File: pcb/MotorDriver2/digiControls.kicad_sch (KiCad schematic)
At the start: 11 parts, among them U3 XIAO-ESP32-C5-DIP, U4 MCP2562FDT-H/SN, U5 MCP2562FDT-H/SN

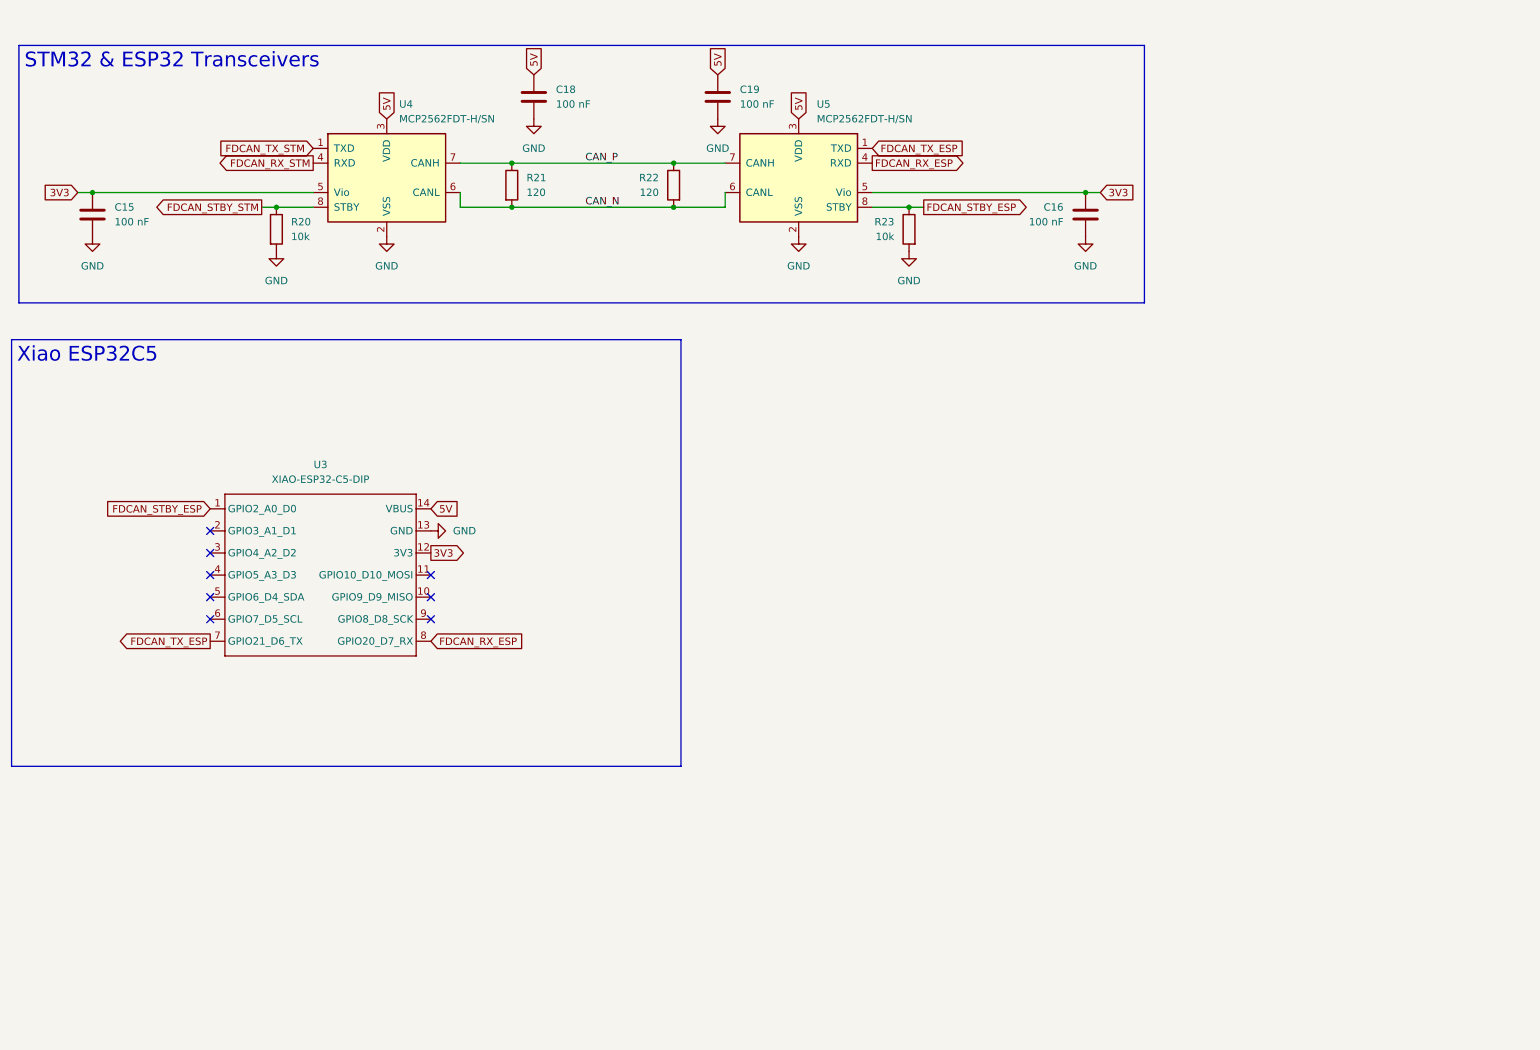
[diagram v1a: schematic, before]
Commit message: added ideal diode protection
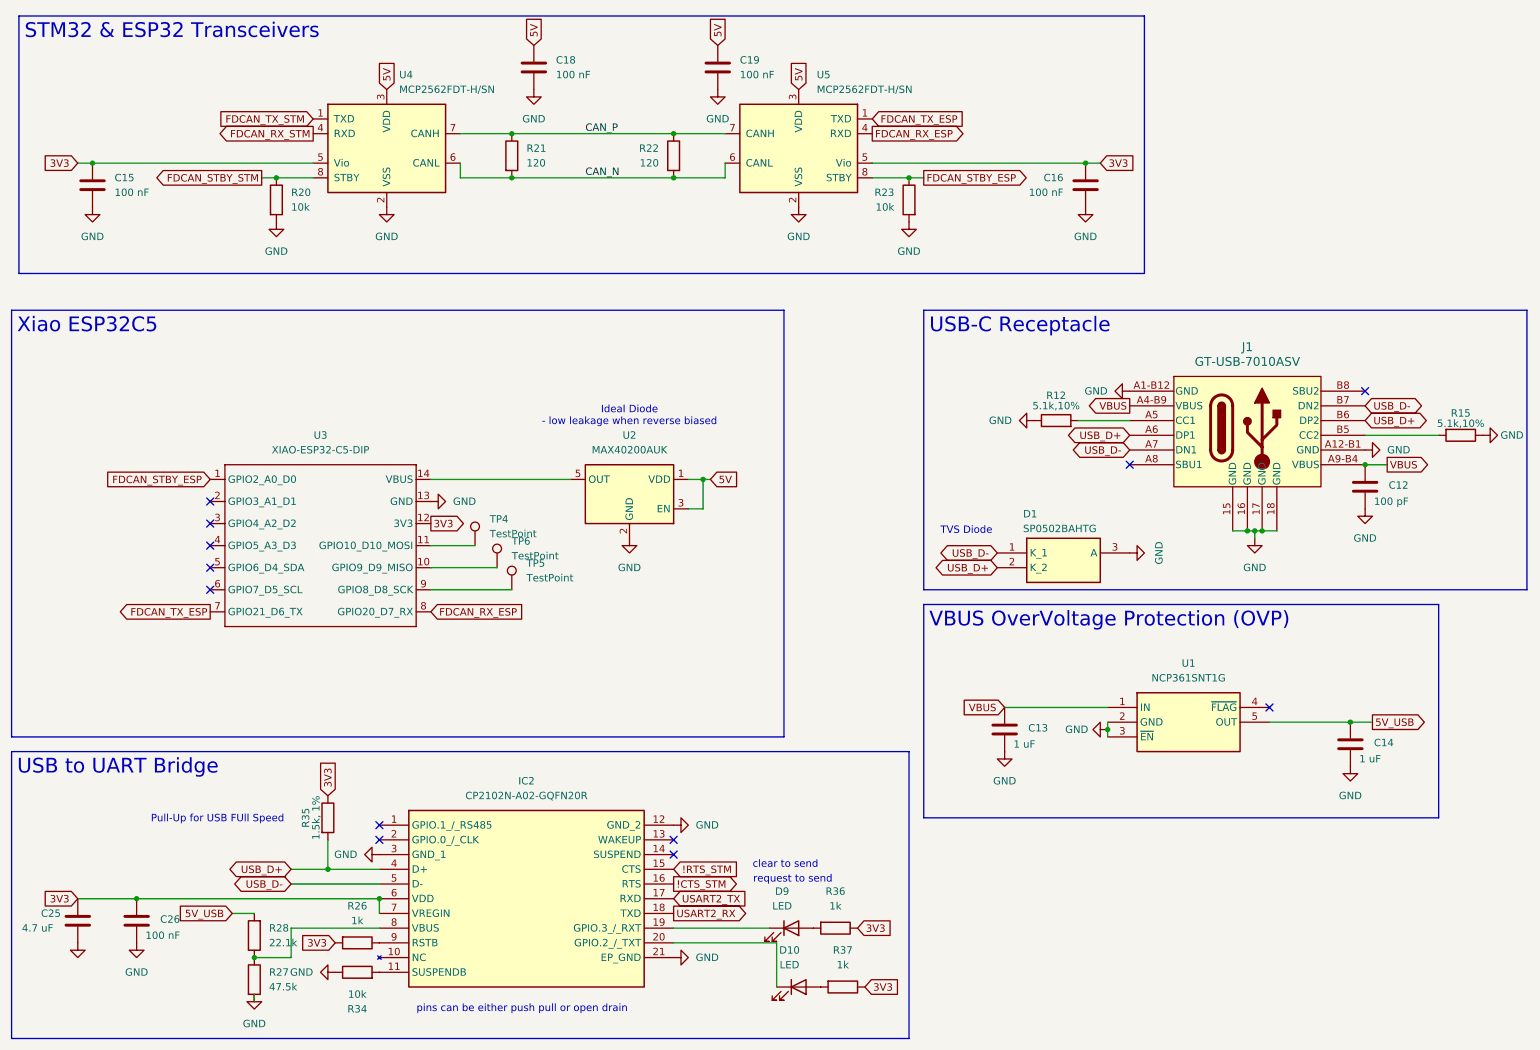
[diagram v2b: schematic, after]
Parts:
- added C12: 100 pF, Capacitor_SMD:C_0402_1005Metric, symbol Device:C
- added C13, C14: 1 uF, Capacitor_SMD:C_0603_1608Metric, symbol Device:C
- added C25: 4.7 uF, Capacitor_SMD:C_0603_1608Metric, symbol Device:C
- added C26: 100 nF, Capacitor_SMD:C_0402_1005Metric, symbol Device:C
- added D1: SP0502BAHTG, CapstoneFootprints:SOT95P237X112-3N, symbol pcb:SP0502BAHTG
- added D10, D9: LED, Diode_SMD:D_0402_1005Metric, symbol Device:LED
- added IC2: CP2102N-A02-GQFN20R, CapstoneFootprints:CP2102NA02GQFN20, symbol pcb:CP2102N-A02-GQFN20R
- added J1: GT-USB-7010ASV, footprintLib:USB4110-GF-A_GCT, symbol pcb:USB4110-GF-A
- added R12, R15: 5.1k,10%, Resistor_SMD:R_0402_1005Metric, symbol Device:R
- added R26, R36, R37: 1k, Resistor_SMD:R_0402_1005Metric, symbol Device:R
- added R27: 47.5k, Resistor_SMD:R_0402_1005Metric, symbol Device:R
- added R28: 22.1k, Resistor_SMD:R_0402_1005Metric, symbol Device:R
- added R34: 10k, Resistor_SMD:R_0402_1005Metric, symbol Device:R
- added R35: 1.5k, 1%, Resistor_SMD:R_0402_1005Metric, symbol Device:R
- added TP4, TP5, TP6: TestPoint, TestPoint:TestPoint_Pad_1.0x1.0mm, symbol Connector:TestPoint
- added U1: NCP361SNT1G, footprintLib:SOT95P275X110-5N, symbol pcb:NCP361SNT1G
- added U2: MAX40200AUK, Package_TO_SOT_SMD:SOT-23-5, symbol Analog_Switch:MAX40200AUK
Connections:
- net 3V3: now also C25.2, C26.2, IC2.6 (VDD), IC2.7 (VREGIN), R26.2, R35.1, R36.1, R37.1
- net 5V: now also U2.1 (VDD), U2.3 (EN); no longer U3.14 (VBUS)
- net GND: now also C12.1, C13.1, C14.1, C25.1, C26.1, D1.3 (A), IC2.12 (GND_2), IC2.21 (EP_GND), IC2.3 (GND_1), J1.15 (GND), J1.16 (GND), J1.17 (GND), J1.18 (GND), J1.A1-B12 (GND), J1.A12-B1 (GND), R12.1, R15.1, R27.2, R34.1, U1.2 (GND), U1.3 (~{EN}), U2.2 (GND)
- net at U3.10 (GPIO9_D9_MISO): now also TP6.1
- net at U3.11 (GPIO10_D10_MOSI): now also TP4.1
- net at U3.9 (GPIO8_D8_SCK): now also TP5.1
- new net: J1.A5 (CC1), R12.2
- new net: IC2.11 (SUSPENDB), R34.2
- new net: D9.1 (K), IC2.19 (GPIO.3_/_RXT)
- new net: D10.1 (K), IC2.20 (GPIO.2_/_TXT)
- new net: IC2.8 (VBUS), R27.1, R28.1
- new net: IC2.9 (RSTB), R26.1
- new net: J1.B5 (CC2), R15.2
- new net: D9.2 (A), R36.2
- new net: D10.2 (A), R37.2
- new net: U2.5 (OUT), U3.14 (VBUS)
- new net !CTS_STM: IC2.16 (RTS)
- new net !RTS_STM: IC2.15 (CTS)
- new net 5V_USB: C14.2, R28.2, U1.5 (OUT)
- new net USART2_RX: IC2.18 (TXD)
- new net USART2_TX: IC2.17 (RXD)
- new net USB_D+: D1.2 (K_2), IC2.4 (D+), J1.A6 (DP1), J1.B6 (DP2), R35.2
- new net USB_D-: D1.1 (K_1), IC2.5 (D-), J1.A7 (DN1), J1.B7 (DN2)
- new net VBUS: C12.2, C13.2, J1.A4-B9 (VBUS), J1.A9-B4 (VBUS), U1.1 (IN)
- no-connect marks 8 -> 12
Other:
- note added: "Ideal Diode - low leakage when reverse biased"
- note added: "Pull-Up for USB FUll Speed"
- note added: "TVS Diode"
- note added: "clear to send"
- note added: "pins can be either push pull or open drain"
- note added: "request to send"
- moved on the sheet: C15, C16, C18, C19, R20, R21, R22, R23, U3, U4, U5

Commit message: Laying out PCB
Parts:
- removed TP4, TP5, TP6: TestPoint, TestPoint:TestPoint_Pad_1.0x1.0mm, symbol Connector:TestPoint
- C13, C14: LCSC (none) -> C15849
- J1: footprint footprintLib:USB4110-GF-A_GCT -> CapstoneFootprints:USB4110-GF-A_GCT
- R12, R15: LCSC (none) -> C25905
- R21, R22: LCSC (none) -> C25079
- U1: footprint footprintLib:SOT95P275X110-5N -> CapstoneFootprints:SOT95P275X110-5N
- U3: footprint footprintLib:XIAO-ESP32-C5-DIP -> CapstoneFootprints:XIAO-ESP32-C5-DIP
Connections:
- no-connect marks 12 -> 15

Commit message: Finished pcb layout
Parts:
- removed D1: SP0502BAHTG, CapstoneFootprints:SOT95P237X112-3N, symbol pcb:SP0502BAHTG
- added U7: USBLC6-2SC6, Package_TO_SOT_SMD:SOT-23-6, symbol Power_Protection:USBLC6-2SC6
- J1: value GT-USB-7010ASV -> USB4110-GF-A
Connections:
- net 5V_USB: no longer R28.2
- net GND: now also U7.2 (GND)
- net USB_D+: now also U7.1 (I/O1), U7.6 (I/O1)
- net USB_D-: now also U7.3 (I/O2), U7.4 (I/O2)
- net VBUS: now also R28.2, U7.5 (VBUS)

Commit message: Removed can transceivers, replaced with spi
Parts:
- removed C15, C16, C18, C19: 100 nF, Capacitor_SMD:C_0402_1005Metric, symbol Device:C
- removed R20, R23: 10k, Resistor_SMD:R_0402_1005Metric, symbol Device:R
- removed R21, R22: 120, Resistor_SMD:R_0402_1005Metric, symbol Device:R
- removed U4, U5: MCP2562FDT-H/SN, Package_SO:SOIC-8_3.9x4.9mm_P1.27mm, symbol Interface_CAN_LIN:MCP2562-H-SN
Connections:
- net SPI2_MISO: now reaches U3.10 (GPIO9_D9_MISO)
- net SPI2_MOSI: now reaches U3.11 (GPIO10_D10_MOSI)
- net CS: now reaches U3.3 (GPIO4_A2_D2)
- net SPI2_SCK: now reaches U3.9 (GPIO8_D8_SCK)
- net FDCAN_RX_ESP: no longer names the net of U3.8 (GPIO20_D7_RX)
- net FDCAN_STBY_ESP: no longer names the net of U3.1 (GPIO2_A0_D0)
- net FDCAN_TX_ESP: no longer names the net of U3.7 (GPIO21_D6_TX)
- no-connect marks 15 -> 14

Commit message: Added step files
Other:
- moved on the sheet: C25, C26, D10, D9, IC2, R26, R27, R28, R34, R35, R36, R37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
